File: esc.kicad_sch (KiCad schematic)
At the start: 66 parts, among them Q10 NMOS, Q5 NMOS, Q6 NMOS, Q7 NMOS, Q8 NMOS, Q9 NMOS, U16 DRV8328ARUYR, U20 STM32G071GBU6, U7 INA190A3IDCKR

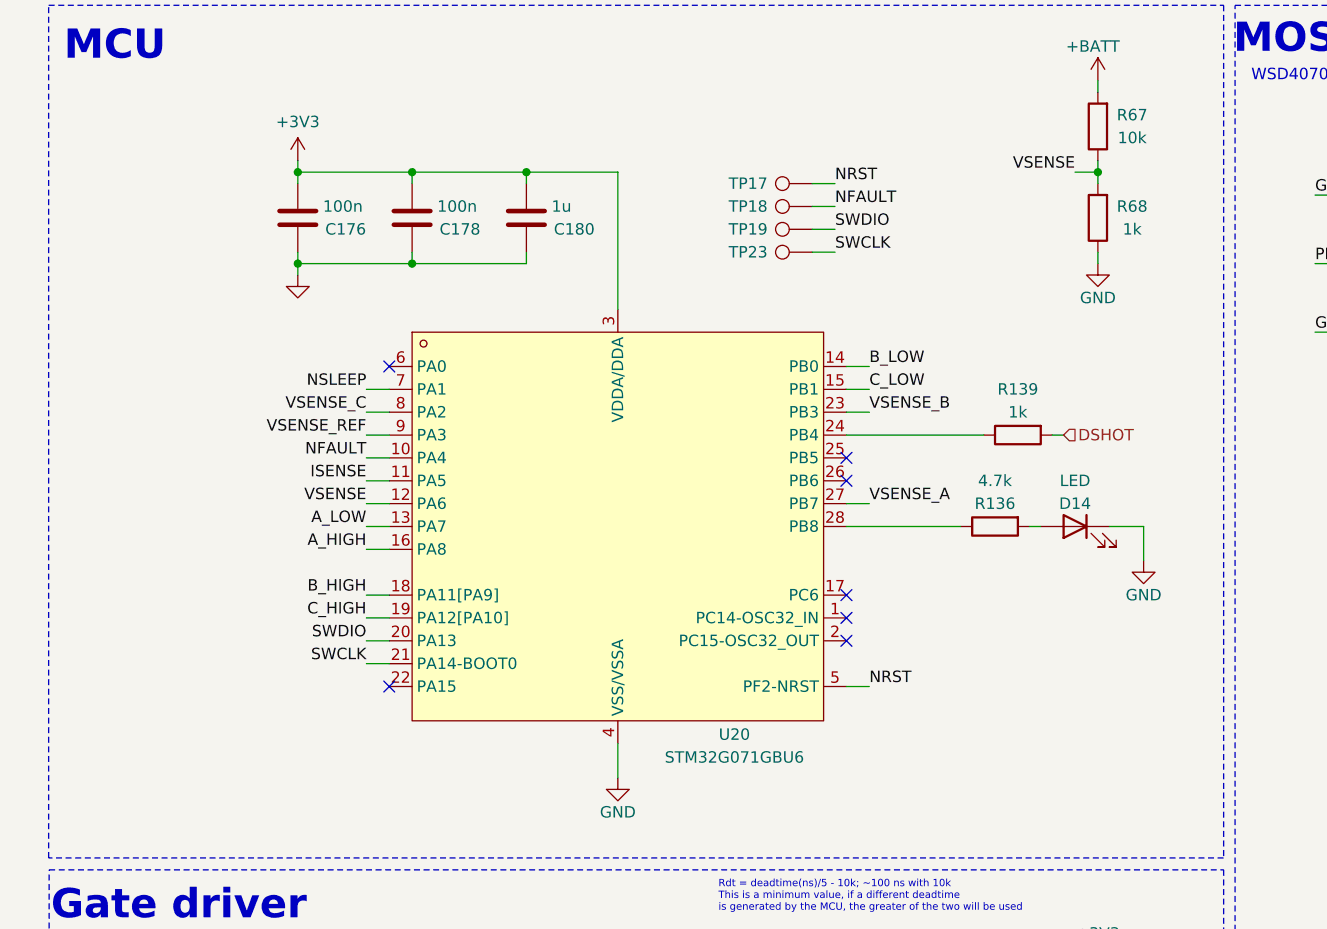
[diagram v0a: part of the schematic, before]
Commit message: Remove extra copper layers
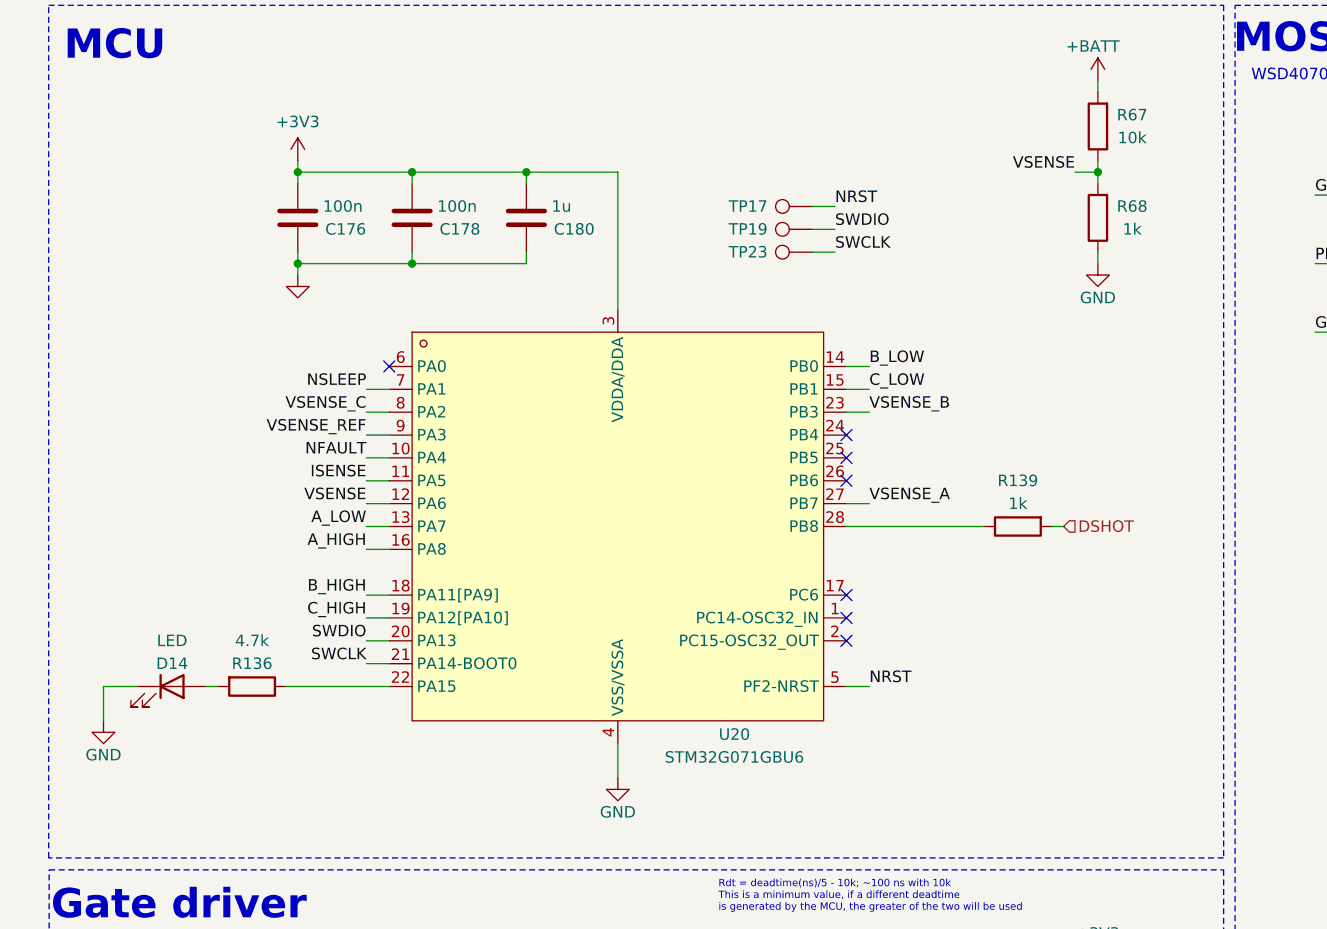
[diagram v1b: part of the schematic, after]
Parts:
- removed TP18: TestPoint, easyeda2kicad:TestPoint_Pad_D1.0mm_No_Courtyard, symbol Connector:TestPoint
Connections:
- net at R139.1: now also U20.28 (PB8); no longer U20.24 (PB4)
- net at U20.22 (PA15): now also R136.1
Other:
- moved on the sheet: D14, R136, R139, TP17
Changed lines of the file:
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@@
 	)
 	(no_connect
-		(at 50.8 88.9)
-	)
-	(no_connect
 		(at 101.6 83.82)
 	)
@@
 	)
 	(no_connect
+		(at 101.6 60.96)
+	)
+	(no_connect
 		(at 101.6 78.74)
 	)
@@
 	(wire
 		(pts
-			(xy 114.3 71.12) (xy 101.6 71.12)
-		)
-		(stroke
-			(width 0)
-			(type default)
-		)
-	)
-	(wire
-		(pts
 			(xy 179.07 83.82) (xy 184.15 83.82)
 		)
@@
 	(wire
 		(pts
+			(xy 39.37 88.9) (xy 50.8 88.9)
+		)
+		(stroke
+			(width 0)
+			(type default)
+		)
+	)
+	(wire
+		(pts
 			(xy 194.31 153.67) (xy 194.31 154.94)
 		)
@@
 	(wire
 		(pts
-			(xy 101.6 60.96) (xy 116.84 60.96)
-		)
-		(stroke
-			(width 0)
-			(type default)
-		)
-	)
-	(wire
-		(pts
 			(xy 203.2 96.52) (xy 214.63 96.52)
 		)
@@
 	(wire
 		(pts
-			(xy 97.79 33.02) (xy 100.33 33.02)
+			(xy 97.79 35.56) (xy 100.33 35.56)
 		)
 		(stroke
@@
 	(wire
 		(pts
+			(xy 101.6 71.12) (xy 116.84 71.12)
+		)
+		(stroke
+			(width 0)
+			(type default)
+		)
+	)
+	(wire
+		(pts
 			(xy 193.04 69.85) (xy 193.04 72.39)
 		)
@@
 	(wire
 		(pts
-			(xy 134.62 71.12) (xy 134.62 74.93)
+			(xy 19.05 88.9) (xy 19.05 92.71)
 		)
 		(stroke
@@
 	(wire
 		(pts
-			(xy 97.79 35.56) (xy 100.33 35.56)
-		)
-		(stroke
-			(width 0)
-			(type default)
-		)
-	)
-	(wire
-		(pts
 			(xy 107.95 135.89) (xy 107.95 139.7)
 		)
@@
 	(wire
 		(pts
-			(xy 130.81 71.12) (xy 134.62 71.12)
+			(xy 22.86 88.9) (xy 19.05 88.9)
 		)
 		(stroke
@@
 	(wire
 		(pts
-			(xy 121.92 71.12) (xy 123.19 71.12)
+			(xy 31.75 88.9) (xy 30.48 88.9)
 		)
 		(stroke
@@
 	(wire
 		(pts
-			(xy 124.46 60.96) (xy 125.73 60.96)
+			(xy 124.46 71.12) (xy 125.73 71.12)
 		)
 		(stroke
@@
 	)
 	(label "NRST"
-		(at 100.33 33.02 0)
+		(at 100.33 35.56 0)
 		(effects
 			(font
@@
 		)
 	)
-	(label "NFAULT"
-		(at 100.33 35.56 0)
-		(effects
-			(font
-				(size 1.27 1.27)
-			)
-			(justify left bottom)
-		)
-	)
 	(label "ISENSE"
 		(at 48.26 66.04 180)
@@
 	(hierarchical_label "DSHOT"
 		(shape input)
-		(at 125.73 60.96 0)
+		(at 125.73 71.12 0)
 		(effects
 			(font
@@
 	)
 	(symbol
-		(lib_id "Connector:TestPoint")
-		(at 97.79 35.56 90)
-		(unit 1)
-		(body_style 1)
-		(exclude_from_sim no)
-		(in_bom yes)
-		(on_board yes)
-		(in_pos_files yes)
-		(dnp no)
-		(property "Reference" "TP18"
-			(at 90.678 35.56 90)
-			(show_name no)
-			(do_not_autoplace no)
-			(effects
-				(font
-					(size 1.27 1.27)
-				)
-			)
-		)
-		(property "Value" "TestPoint"
-			(at 94.488 33.02 90)
-			(hide yes)
-			(show_name no)
-			(do_not_autoplace no)
-			(effects
-				(font
-					(size 1.27 1.27)
-				)
-			)
-		)
-		(property "Footprint" "easyeda2kicad:TestPoint_Pad_D1.0mm_No_Courtyard"
-			(at 97.79 30.48 0)
-			(hide yes)
-			(show_name no)
-			(do_not_autoplace no)
-			(effects
-				(font
-					(size 1.27 1.27)
-				)
-			)
-		)
-		(property "Datasheet" ""
-			(at 97.79 30.48 0)
-			(hide yes)
-			(show_name no)
-			(do_not_autoplace no)
-			(effects
-				(font
-					(size 1.27 1.27)
-				)
-			)
-		)
-		(property "Description" "test point"
-			(at 97.79 35.56 0)
-			(hide yes)
-			(show_name no)
-			(do_not_autoplace no)
-			(effects
-				(font
-					(size 1.27 1.27)
-				)
-			)
-		)
-		(pin "1"
-		)
-		(instances
-			(project "espdrone"
-				(path "/d7b09c1f-60ff-44c2-9b85-8e9b4c9b8de4/3f1ec40b-2861-4856-8c91-e3c961c5da6f"
-					(reference "TP30")
-					(unit 1)
-				)
-				(path "/d7b09c1f-60ff-44c2-9b85-8e9b4c9b8de4/51921b67-4a63-4a4a-adc0-e4b24a3252b8"
-					(reference "TP54")
-					(unit 1)
-				)
-				(path "/d7b09c1f-60ff-44c2-9b85-8e9b4c9b8de4/54db73ba-97d3-488f-8063-7cfc3cee66e2"
-					(reference "TP42")
-					(unit 1)
-				)
-				(path "/d7b09c1f-60ff-44c2-9b85-8e9b4c9b8de4/e73f72f2-28de-4d9d-8e81-9b095eab4bb5"
-					(reference "TP18")
-					(unit 1)
-				)
-			)
-		)
-	)
-	(symbol
 		(lib_name "GND_2")
 		(lib_id "power:GND")
-		(at 134.62 74.93 0)
-		(mirror y)
+		(at 19.05 92.71 0)
 		(unit 1)
 		(body_style 1)
@@
 		(dnp no)
 		(property "Reference" "#PWR0260"
-			(at 134.62 81.28 0)
+			(at 19.05 99.06 0)
 			(hide yes)
 			(show_name no)
@@
 		)
 		(property "Value" "GND"
-			(at 134.62 78.74 0)
+			(at 19.05 96.52 0)
 			(show_name no)
 			(do_not_autoplace no)
@@
 		)
 		(property "Footprint" ""
-			(at 134.62 74.93 0)
+			(at 19.05 92.71 0)
 			(hide yes)
 			(show_name no)
@@
 		)
 		(property "Datasheet" ""
-			(at 134.62 74.93 0)
+			(at 19.05 92.71 0)
 			(hide yes)
 			(show_name no)
@@
 		)
 		(property "Description" "Power symbol creates a global label with name \"GND\" , ground"
-			(at 134.62 74.93 0)
+			(at 19.05 92.71 0)
 			(hide yes)
 			(show_name no)
@@
 	(symbol
 		(lib_id "Device:R")
-		(at 120.65 60.96 90)
+		(at 120.65 71.12 90)
 		(mirror x)
 		(unit 1)
@@
 		(dnp no)
 		(property "Reference" "R139"
-			(at 120.65 55.88 90)
+			(at 120.65 66.04 90)
 			(show_name no)
 			(do_not_autoplace no)
@@
 		)
 		(property "Value" "1k"
-			(at 120.65 58.42 90)
+			(at 120.65 68.58 90)
 			(show_name no)
 			(do_not_autoplace no)
@@
 		)
 		(property "Footprint" "Resistor_SMD:R_0201_0603Metric"
-			(at 120.65 59.182 90)
+			(at 120.65 69.342 90)
 			(hide yes)
 			(show_name no)
@@
 		)
 		(property "Datasheet" ""
-			(at 120.65 60.96 0)
+			(at 120.65 71.12 0)
 			(hide yes)
 			(show_name no)
@@
 		)
 		(property "Description" "Resistor"
-			(at 120.65 60.96 0)
+			(at 120.65 71.12 0)
 			(hide yes)
 			(show_name no)
@@
 	(symbol
 		(lib_id "Device:LED")
-		(at 127 71.12 0)
-		(mirror y)
+		(at 26.67 88.9 0)
 		(unit 1)
 		(body_style 1)
@@
 		(dnp no)
 		(property "Reference" "D14"
-			(at 127 68.58 0)
+			(at 26.67 86.36 0)
 			(show_name no)
 			(do_not_autoplace no)
@@
 		)
 		(property "Value" "LED"
-			(at 127 66.04 0)
+			(at 26.67 83.82 0)
 			(show_name no)
 			(do_not_autoplace no)
@@
 		)
 		(property "Footprint" "LED_SMD:LED_0402_1005Metric"
-			(at 127 71.12 0)
+			(at 26.67 88.9 0)
 			(hide yes)
 			(show_name no)
@@
 		)
 		(property "Datasheet" ""
-			(at 127 71.12 0)
+			(at 26.67 88.9 0)
 			(hide yes)
 			(show_name no)
@@
 		)
 		(property "Description" "Light emitting diode"
-			(at 127 71.12 0)
+			(at 26.67 88.9 0)
 			(hide yes)
 			(show_name no)
@@
 		)
 		(property "Sim.Pins" "1=K 2=A"
-			(at 127 71.12 0)
+			(at 26.67 88.9 0)
 			(hide yes)
 			(show_name no)
@@
 	(symbol
 		(lib_id "Device:R")
-		(at 118.11 71.12 90)
-		(mirror x)
+		(at 35.56 88.9 270)
 		(unit 1)
 		(body_style 1)
@@
 		(dnp no)
 		(property "Reference" "R136"
-			(at 118.11 68.58 90)
+			(at 35.56 86.36 90)
 			(show_name no)
 			(do_not_autoplace no)
@@
 		)
 		(property "Value" "4.7k"
-			(at 118.11 66.04 90)
+			(at 35.56 83.82 90)
 			(show_name no)
 			(do_not_autoplace no)
@@
 		)
 		(property "Footprint" "Resistor_SMD:R_0201_0603Metric"
-			(at 118.11 69.342 90)
+			(at 35.56 87.122 90)
 			(hide yes)
 			(show_name no)
@@
 		)
 		(property "Datasheet" ""
-			(at 118.11 71.12 0)
+			(at 35.56 88.9 0)
 			(hide yes)
 			(show_name no)
@@
 		)
 		(property "Description" "Resistor"
-			(at 118.11 71.12 0)
+			(at 35.56 88.9 0)
 			(hide yes)
 			(show_name no)
@@
 	(symbol
 		(lib_id "Connector:TestPoint")
-		(at 97.79 33.02 90)
+		(at 97.79 35.56 90)
 		(unit 1)
 		(body_style 1)
@@
 		(dnp no)
 		(property "Reference" "TP17"
-			(at 90.678 33.02 90)
+			(at 90.678 35.56 90)
 			(show_name no)
 			(do_not_autoplace no)
@@
 		)
 		(property "Value" "TestPoint"
-			(at 94.488 30.48 90)
+			(at 94.488 33.02 90)
 			(hide yes)
 			(show_name no)
@@
 		)
 		(property "Footprint" "easyeda2kicad:TestPoint_Pad_D1.0mm_No_Courtyard"
-			(at 97.79 27.94 0)
+			(at 97.79 30.48 0)
 			(hide yes)
 			(show_name no)
@@
 		)
 		(property "Datasheet" ""
-			(at 97.79 27.94 0)
+			(at 97.79 30.48 0)
 			(hide yes)
 			(show_name no)
@@
 		)
 		(property "Description" "test point"
-			(at 97.79 33.02 0)
+			(at 97.79 35.56 0)
 			(hide yes)
 			(show_name no)

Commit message: Reduce ESC LED size to 0201
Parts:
- D14: footprint LED_SMD:LED_0402_1005Metric -> LED_SMD:LED_0201_0603Metric
- R62: footprint Resistor_SMD:R_0201_0603Metric -> Resistor_SMD:R_0402_1005Metric
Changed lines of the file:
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@@
 			)
 		)
-		(property "Footprint" "Resistor_SMD:R_0201_0603Metric"
+		(property "Footprint" "Resistor_SMD:R_0402_1005Metric"
 			(at 44.45 155.448 90)
 			(hide yes)
@@
 			)
 		)
-		(property "Footprint" "LED_SMD:LED_0402_1005Metric"
+		(property "Footprint" "LED_SMD:LED_0201_0603Metric"
 			(at 26.67 88.9 0)
 			(hide yes)

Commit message: Funny 45 degree ESC layout
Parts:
- removed C117: 100n, Capacitor_SMD:C_0201_0603Metric, symbol Device:C
- removed C119: 1n, Capacitor_SMD:C_0201_0603Metric, symbol Device:C
- removed R67: 10k, Resistor_SMD:R_0201_0603Metric, symbol Device:R
- removed R68, R72: 1k, Resistor_SMD:R_0201_0603Metric, symbol Device:R
- removed R71: 0.001, Resistor_SMD:R_1206_3216Metric, symbol Device:R
- removed U7: INA190A3IDCKR, easyeda2kicad:SC-70-6_L2.0-W1.3-P0.65-LS2.1-BL, symbol easyeda2kicad:INA190A3IDCKR
- C109, C110, C111: footprint Capacitor_SMD:C_0603_1608Metric -> Capacitor_SMD:C_0402_1005Metric
- R62: footprint Resistor_SMD:R_0402_1005Metric -> Resistor_SMD:R_0201_0603Metric
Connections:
- net LSS is gone; now on net GND: Q10.3 (S), Q6.3 (S), Q8.3 (S), U16.17 (LSS)
- net VSENSE is gone; now on net NFAULT: U20.12 (PA6)
- net NFAULT: no longer U20.10 (PA4)
- net NSLEEP: now also U20.10 (PA4); no longer U20.7 (PA1)
- net ISENSE: no longer names the net of U20.11 (PA5)
- no-connect marks 7 -> 9
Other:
- note removed: "Route as 4-wire kelvin shunt!"
- moved on the sheet: C113, C114, C116, C118, C120, C121, C122, C123, C124, C125, C198, C202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

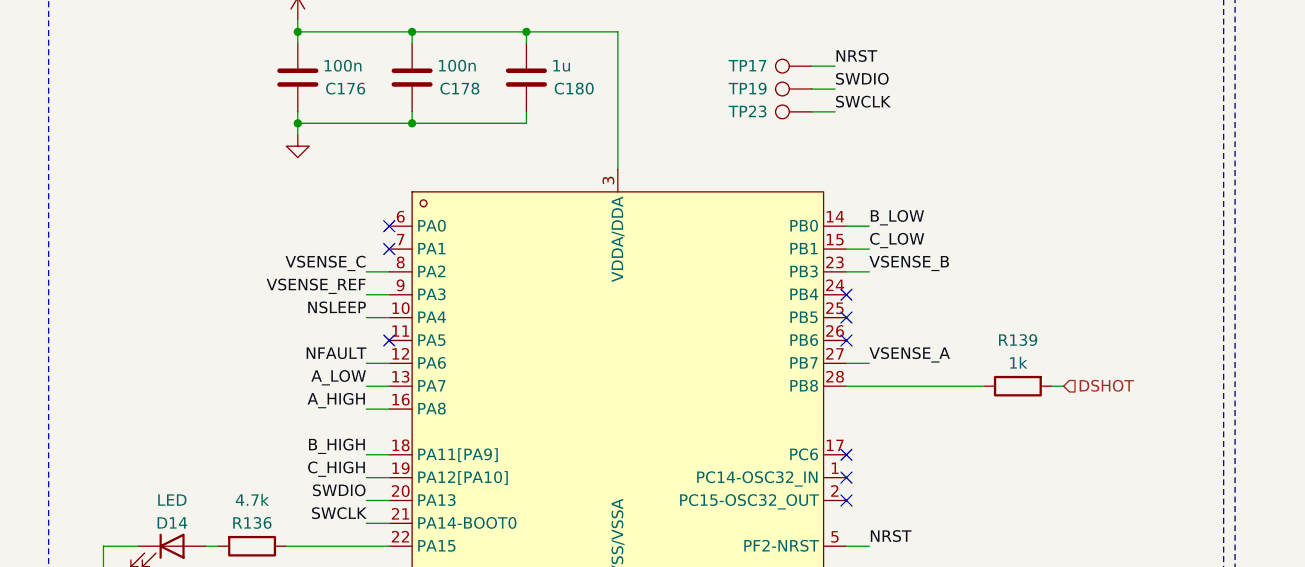
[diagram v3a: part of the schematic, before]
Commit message: Add motor pad vias
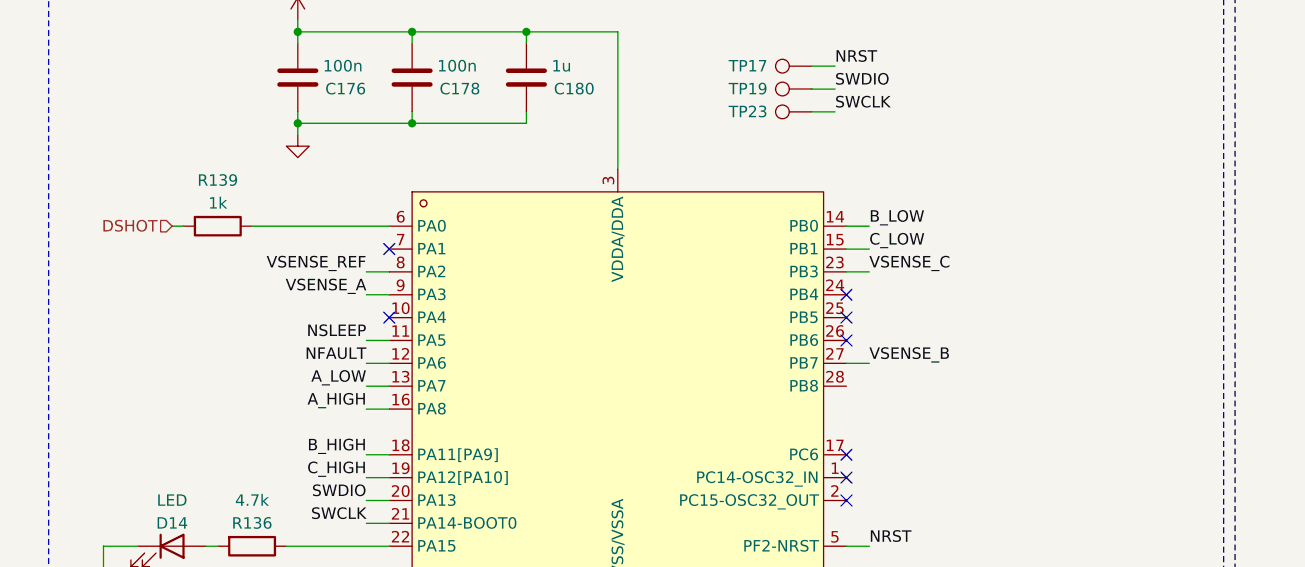
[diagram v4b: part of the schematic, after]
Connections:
- net NSLEEP: now also U20.11 (PA5); no longer U20.10 (PA4)
- net VSENSE_A: now also U20.9 (PA3); no longer U20.27 (PB7)
- net VSENSE_B: now also U20.27 (PB7); no longer U20.23 (PB3)
- net VSENSE_C: now also U20.23 (PB3); no longer U20.8 (PA2)
- net VSENSE_REF: now also U20.8 (PA2); no longer U20.9 (PA3)
- net at R139.1: now also U20.6 (PA0); no longer U20.28 (PB8)
- no-connect marks 9 -> 8
